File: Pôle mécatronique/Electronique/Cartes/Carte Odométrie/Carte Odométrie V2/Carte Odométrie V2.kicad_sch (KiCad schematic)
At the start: 7 parts, among them J1 Conn_01x05, J2 Conn_01x08, J3 Conn_01x07, J4 Conn_01x04, J5 Conn_01x07, U1 TCAN332

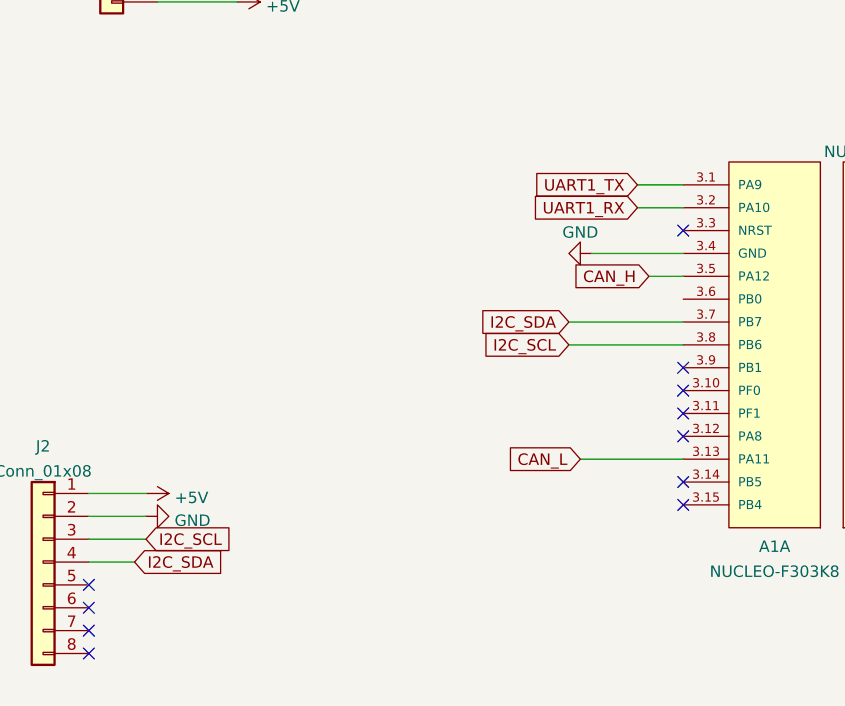
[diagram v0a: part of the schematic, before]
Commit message: carte odométrie avec resistance pull up
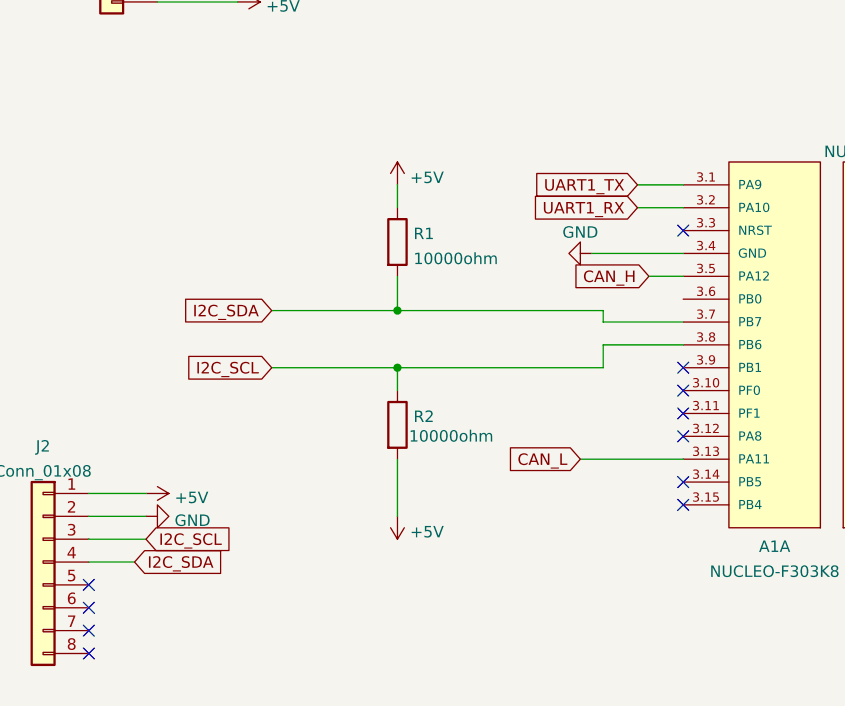
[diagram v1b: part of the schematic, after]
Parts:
- added R1, R2: 10000ohm, Resistor_THT:R_Axial_DIN0207_L6.3mm_D2.5mm_P10.16mm_Horizontal, symbol Device:R
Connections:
- net +5V: now also R1.1, R2.2
- net I2C_SCL: now also R2.1
- net I2C_SDA: now also R1.2

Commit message: Carte odométrie v2 "fini"
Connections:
- net CAN_H: now also J4.2 (Pin_2); no longer A1.3.5 (PA12)
- net CAN_L: now also J4.3 (Pin_3); no longer A1.3.13 (PA11)
- net CAN_RX: now also A1.3.5 (PA12); no longer J4.2 (Pin_2)
- net CAN_TX: now also A1.3.13 (PA11); no longer J4.3 (Pin_3)
- net GND: no longer J5.2 (Pin_2)
- net UART1_RX: now also J1.4 (Pin_4); no longer J1.3 (Pin_3)
- net UART1_TX: now also J1.3 (Pin_3); no longer J1.4 (Pin_4)
- net SPI_CS: now reaches A1.4.9 (PA4)
- net SPI_CS: now also J5.2 (Pin_2)
- no-connect marks 22 -> 23
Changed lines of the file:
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@@
   (no_connect (at 58.42 105.41))
   (no_connect (at 157.48 83.82))
-  (no_connect (at 157.48 81.28))
+  (no_connect (at 157.48 71.12))
   (no_connect (at 124.46 66.04))
   (no_connect (at 66.04 30.48))
@@
   (no_connect (at 236.22 140.97))
   (no_connect (at 124.46 96.52))
+  (no_connect (at 157.48 66.04))
   (no_connect (at 124.46 86.36))
   (no_connect (at 124.46 88.9))
@@
     (stroke (width 0) (type default) (color 0 0 0 0))
   )
+  (wire (pts (xy 114.3 71.12) (xy 124.46 71.12))
+    (stroke (width 0) (type default) (color 0 0 0 0))
+  )
   (wire (pts (xy 92.71 91.44) (xy 92.71 97.79))
     (stroke (width 0) (type default) (color 0 0 0 0))
   )
-  (wire (pts (xy 120.65 71.12) (xy 124.46 71.12))
-    (stroke (width 0) (type default) (color 0 0 0 0))
-  )
   (wire (pts (xy 224.79 96.52) (xy 236.22 96.52))
     (stroke (width 0) (type default) (color 0 0 0 0))
   )
+  (wire (pts (xy 226.06 39.37) (xy 232.41 39.37))
+    (stroke (width 0) (type default) (color 0 0 0 0))
+  )
   (wire (pts (xy 115.57 78.74) (xy 124.46 78.74))
     (stroke (width 0) (type default) (color 0 0 0 0))
   )
+  (wire (pts (xy 66.04 35.56) (xy 72.39 35.56))
+    (stroke (width 0) (type default) (color 0 0 0 0))
+  )
   (wire (pts (xy 224.79 128.27) (xy 236.22 128.27))
     (stroke (width 0) (type default) (color 0 0 0 0))
@@
     (stroke (width 0) (type default) (color 0 0 0 0))
   )
+  (wire (pts (xy 157.48 81.28) (xy 165.1 81.28))
+    (stroke (width 0) (type default) (color 0 0 0 0))
+  )
   (wire (pts (xy 58.42 95.25) (xy 64.77 95.25))
     (stroke (width 0) (type default) (color 0 0 0 0))
@@
     (stroke (width 0) (type default) (color 0 0 0 0))
   )
+  (wire (pts (xy 66.04 38.1) (xy 72.39 38.1))
+    (stroke (width 0) (type default) (color 0 0 0 0))
+  )
   (wire (pts (xy 119.38 63.5) (xy 124.46 63.5))
     (stroke (width 0) (type default) (color 0 0 0 0))
@@
     (stroke (width 0) (type default) (color 0 0 0 0))
   )
-  (wire (pts (xy 113.03 91.44) (xy 124.46 91.44))
-    (stroke (width 0) (type default) (color 0 0 0 0))
-  )
-  (wire (pts (xy 66.04 38.1) (xy 72.39 38.1))
+  (wire (pts (xy 227.33 36.83) (xy 232.41 36.83))
     (stroke (width 0) (type default) (color 0 0 0 0))
   )
@@
     (stroke (width 0) (type default) (color 0 0 0 0))
   )
-  (wire (pts (xy 66.04 35.56) (xy 72.39 35.56))
-    (stroke (width 0) (type default) (color 0 0 0 0))
-  )
-  (wire (pts (xy 227.33 39.37) (xy 232.41 39.37))
-    (stroke (width 0) (type default) (color 0 0 0 0))
-  )
   (wire (pts (xy 157.48 93.98) (xy 162.56 93.98))
     (stroke (width 0) (type default) (color 0 0 0 0))
@@
     (stroke (width 0) (type default) (color 0 0 0 0))
   )
-  (wire (pts (xy 227.33 88.9) (xy 236.22 88.9))
-    (stroke (width 0) (type default) (color 0 0 0 0))
-  )
   (wire (pts (xy 78.74 74.93) (xy 92.71 74.93))
     (stroke (width 0) (type default) (color 0 0 0 0))
   )
+  (wire (pts (xy 118.11 91.44) (xy 124.46 91.44))
+    (stroke (width 0) (type default) (color 0 0 0 0))
+  )
   (wire (pts (xy 154.94 142.24) (xy 168.91 142.24))
     (stroke (width 0) (type default) (color 0 0 0 0))
@@
     (stroke (width 0) (type default) (color 0 0 0 0))
   )
-  (wire (pts (xy 227.33 36.83) (xy 232.41 36.83))
-    (stroke (width 0) (type default) (color 0 0 0 0))
-  )
   (wire (pts (xy 157.48 73.66) (xy 163.83 73.66))
     (stroke (width 0) (type default) (color 0 0 0 0))
@@
     (stroke (width 0) (type default) (color 0 0 0 0))
   )
+  (wire (pts (xy 213.36 88.9) (xy 236.22 88.9))
+    (stroke (width 0) (type default) (color 0 0 0 0))
+  )
   (wire (pts (xy 125.73 134.62) (xy 129.54 134.62))
     (stroke (width 0) (type default) (color 0 0 0 0))
@@
     )
   )
-  (global_label "CAN_TX" (shape input) (at 227.33 39.37 180) (fields_autoplaced)
-    (effects (font (size 1.27 1.27)) (justify right))
-    (property "Intersheet References" "${INTERSHEET_REFS}" (id 0) (at 218.172 39.2906 0)
+  (global_label "CAN_TX" (shape input) (at 118.11 91.44 180) (fields_autoplaced)
+    (effects (font (size 1.27 1.27)) (justify right))
+    (property "Intersheet References" "${INTERSHEET_REFS}" (id 0) (at 108.952 91.3606 0)
       (effects (font (size 1.27 1.27)) (justify right) hide)
     )
@@
     )
   )
-  (global_label "CAN_RX" (shape input) (at 227.33 36.83 180) (fields_autoplaced)
-    (effects (font (size 1.27 1.27)) (justify right))
-    (property "Intersheet References" "${INTERSHEET_REFS}" (id 0) (at 217.8696 36.7506 0)
-      (effects (font (size 1.27 1.27)) (justify right) hide)
-    )
-  )
-  (global_label "CAN_H" (shape input) (at 120.65 71.12 180) (fields_autoplaced)
-    (effects (font (size 1.27 1.27)) (justify right))
-    (property "Intersheet References" "${INTERSHEET_REFS}" (id 0) (at 112.3387 71.0406 0)
+  (global_label "CAN_RX" (shape input) (at 114.3 71.12 180) (fields_autoplaced)
+    (effects (font (size 1.27 1.27)) (justify right))
+    (property "Intersheet References" "${INTERSHEET_REFS}" (id 0) (at 104.8396 71.0406 0)
+      (effects (font (size 1.27 1.27)) (justify right) hide)
+    )
+  )
+  (global_label "CAN_H" (shape input) (at 227.33 36.83 180) (fields_autoplaced)
+    (effects (font (size 1.27 1.27)) (justify right))
+    (property "Intersheet References" "${INTERSHEET_REFS}" (id 0) (at 219.0187 36.7506 0)
       (effects (font (size 1.27 1.27)) (justify right) hide)
     )
@@
     )
   )
-  (global_label "CAN_L" (shape input) (at 113.03 91.44 180) (fields_autoplaced)
-    (effects (font (size 1.27 1.27)) (justify right))
-    (property "Intersheet References" "${INTERSHEET_REFS}" (id 0) (at 105.021 91.3606 0)
+  (global_label "CAN_L" (shape input) (at 226.06 39.37 180) (fields_autoplaced)
+    (effects (font (size 1.27 1.27)) (justify right))
+    (property "Intersheet References" "${INTERSHEET_REFS}" (id 0) (at 218.051 39.2906 0)
+      (effects (font (size 1.27 1.27)) (justify right) hide)
+    )
+  )
+  (global_label "SPI_CS" (shape input) (at 213.36 88.9 180) (fields_autoplaced)
+    (effects (font (size 1.27 1.27)) (justify right))
+    (property "Intersheet References" "${INTERSHEET_REFS}" (id 0) (at 204.5044 88.9794 0)
       (effects (font (size 1.27 1.27)) (justify right) hide)
     )
@@
     )
   )
+  (global_label "SPI_CS" (shape input) (at 165.1 81.28 0) (fields_autoplaced)
+    (effects (font (size 1.27 1.27)) (justify left))
+    (property "Intersheet References" "${INTERSHEET_REFS}" (id 0) (at 173.9556 81.2006 0)
+      (effects (font (size 1.27 1.27)) (justify left) hide)
+    )
+  )
   (global_label "SPI_MOSI" (shape input) (at 163.83 73.66 0) (fields_autoplaced)
     (effects (font (size 1.27 1.27)) (justify left))
@@
     )
   )
-  (global_label "UART1_TX" (shape input) (at 72.39 38.1 0) (fields_autoplaced)
-    (effects (font (size 1.27 1.27)) (justify left))
-    (property "Intersheet References" "${INTERSHEET_REFS}" (id 0) (at 83.7252 38.0206 0)
-      (effects (font (size 1.27 1.27)) (justify left) hide)
-    )
-  )
-  (global_label "UART1_RX" (shape input) (at 72.39 35.56 0) (fields_autoplaced)
-    (effects (font (size 1.27 1.27)) (justify left))
-    (property "Intersheet References" "${INTERSHEET_REFS}" (id 0) (at 84.0275 35.4806 0)
+  (global_label "UART1_TX" (shape input) (at 72.39 35.56 0) (fields_autoplaced)
+    (effects (font (size 1.27 1.27)) (justify left))
+    (property "Intersheet References" "${INTERSHEET_REFS}" (id 0) (at 83.7252 35.4806 0)
+      (effects (font (size 1.27 1.27)) (justify left) hide)
+    )
+  )
+  (global_label "UART1_RX" (shape input) (at 72.39 38.1 0) (fields_autoplaced)
+    (effects (font (size 1.27 1.27)) (justify left))
+    (property "Intersheet References" "${INTERSHEET_REFS}" (id 0) (at 84.0275 38.0206 0)
       (effects (font (size 1.27 1.27)) (justify left) hide)
     )
@@
     )
     (property "Datasheet" "" (id 3) (at 64.77 97.79 0)
-      (effects (font (size 1.27 1.27)) hide)
-    )
-    (pin "1")
-  )
-  (symbol (lib_id "power:GND") (at 227.33 88.9 270) (mirror x) (unit 1)
-    (in_bom yes) (on_board yes) (fields_autoplaced)
-    (property "Reference" "#PWR0111" (id 0) (at 220.98 88.9 0)
-      (effects (font (size 1.27 1.27)) hide)
-    )
-    (property "Value" "GND" (id 1) (at 224.1551 89.379 90)
-      (effects (font (size 1.27 1.27)) (justify right))
-    )
-    (property "Footprint" "" (id 2) (at 227.33 88.9 0)
-      (effects (font (size 1.27 1.27)) hide)
-    )
-    (property "Datasheet" "" (id 3) (at 227.33 88.9 0)
       (effects (font (size 1.27 1.27)) hide)
     )
@@
       (reference "#PWR0110") (unit 1) (value "GND") (footprint "")
     )
-    (path "/2faa7a86-6cd5-43fb-826d-24fe8aa24d1d"
-      (reference "#PWR0111") (unit 1) (value "GND") (footprint "")
-    )
     (path "/639f0dba-6f1f-4250-a292-2bc84fdc0bd9"
